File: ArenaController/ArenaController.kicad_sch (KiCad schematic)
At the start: 29 parts, among them J1 RJ45, J2 RJ45, J4 RJ45, J5 RJ45, J6 RJ45, J8 Screw_Terminal_01x04, J9 Barrel_Jack_MountingPin, Q1 FS3400, Q2 FS3400, Q3 FS3400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

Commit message: small boardwork cleanup to try and lay it out.
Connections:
- net G_End: now also J4.7; no longer J4.6
- net G_Pause: no longer names the net of U3.25 (RTC_GPIO5/ADC1_7/GPIO35)
- net G_Pause: no longer J4.5
- net G_Reset: no longer names the net of U3.11 (GPIO18/V_SPI_CLK/SCK)
- net G_Reset: no longer J4.7

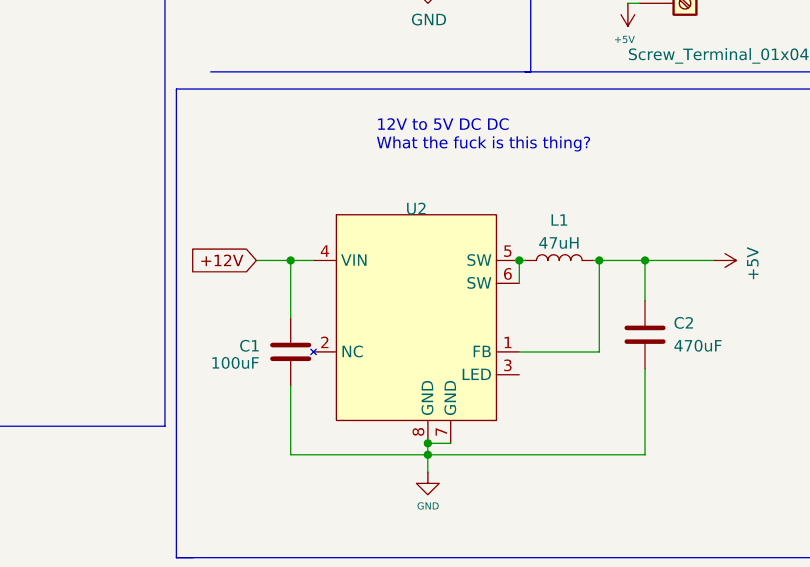
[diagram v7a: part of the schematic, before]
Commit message: Updated layout, added major routing.  Still need connector for the WS2812B output and pin relayout.
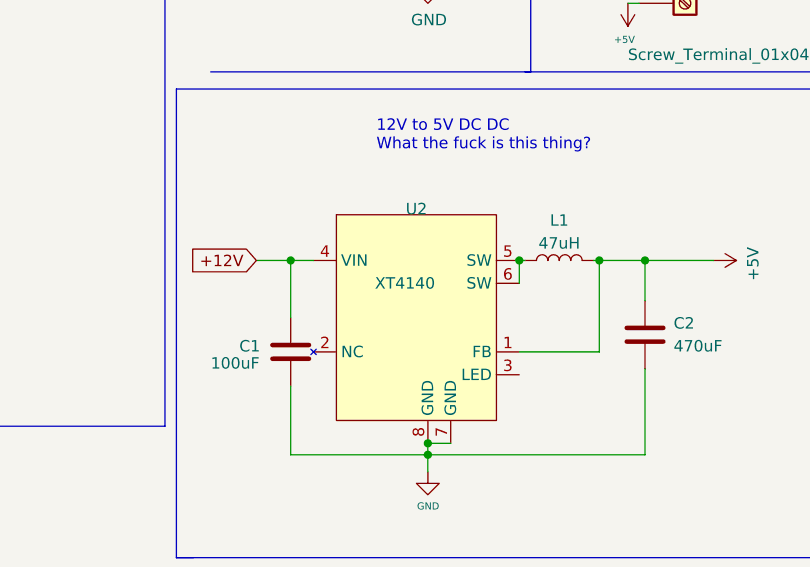
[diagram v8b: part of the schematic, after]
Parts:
- U2: value ~ -> XT4140
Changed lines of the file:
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@@
       (effects (font (size 1.27 1.27)))
     )
-    (property "Value" "~" (at 139.7 126.365 0)
+    (property "Value" "XT4140" (at 139.7 126.365 0)
       (effects (font (size 1.27 1.27)))
     )
